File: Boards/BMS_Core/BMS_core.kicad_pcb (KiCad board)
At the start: 2 copper layers, 61 x 80 mm, 79 parts, among them IC1 ATMEGA16M1, J1 CONN_02X03, J2 B5B-PH-K-S, J3 MM_F_VT_20, J4 MicroFit_V_2, J5 isoSPI-Cutout, K1 G5Q-1A4-DC12, Q1 SSM3K333R, T1 T_LAN_SM91501ALE, U1 MCP2561-E_SN, U2 SN74LVC1G17, U3 LTC6820HMS, U4 MCP6001, U5 MCP6001, U6 MCP6001, U7 SN74LVC1G32, U8 TPS560430YF, Y1 Crystal_SMD

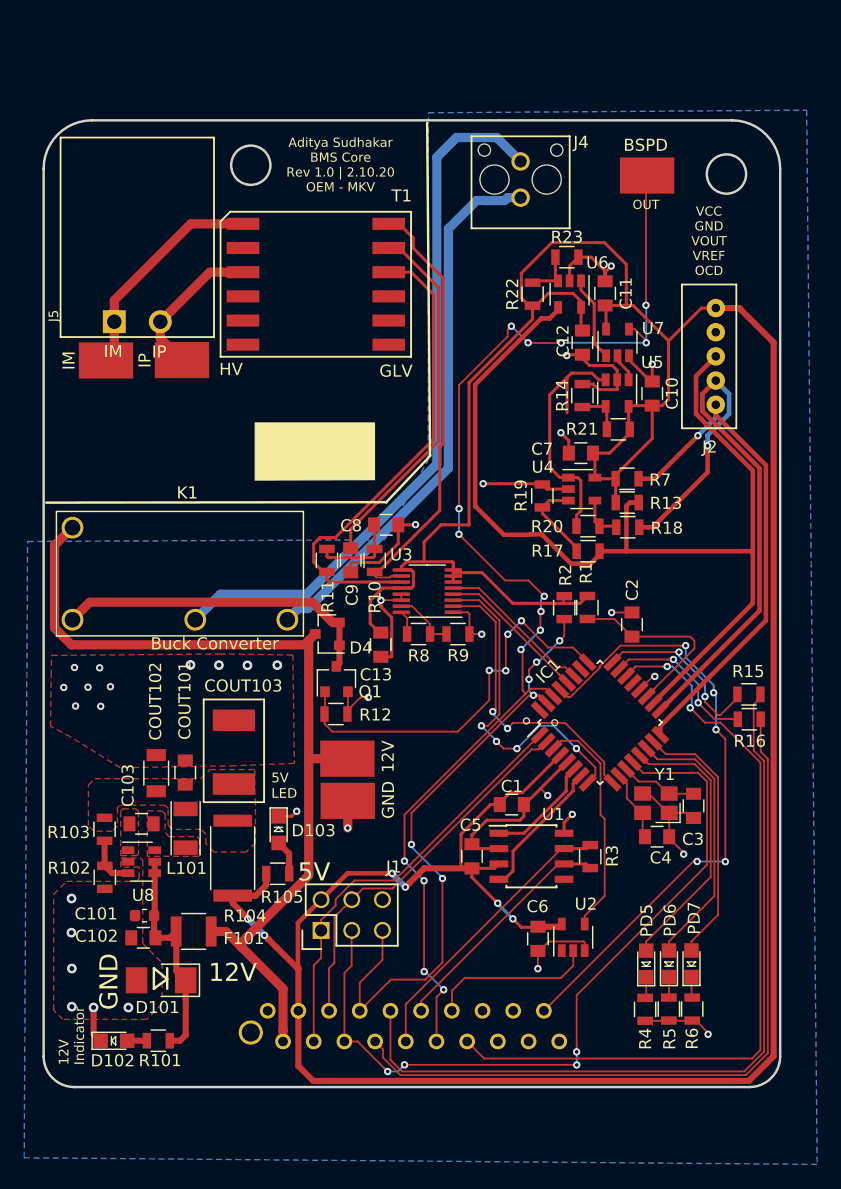
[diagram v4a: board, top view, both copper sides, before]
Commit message: New BMS core DXF, proper GLV HV spacing
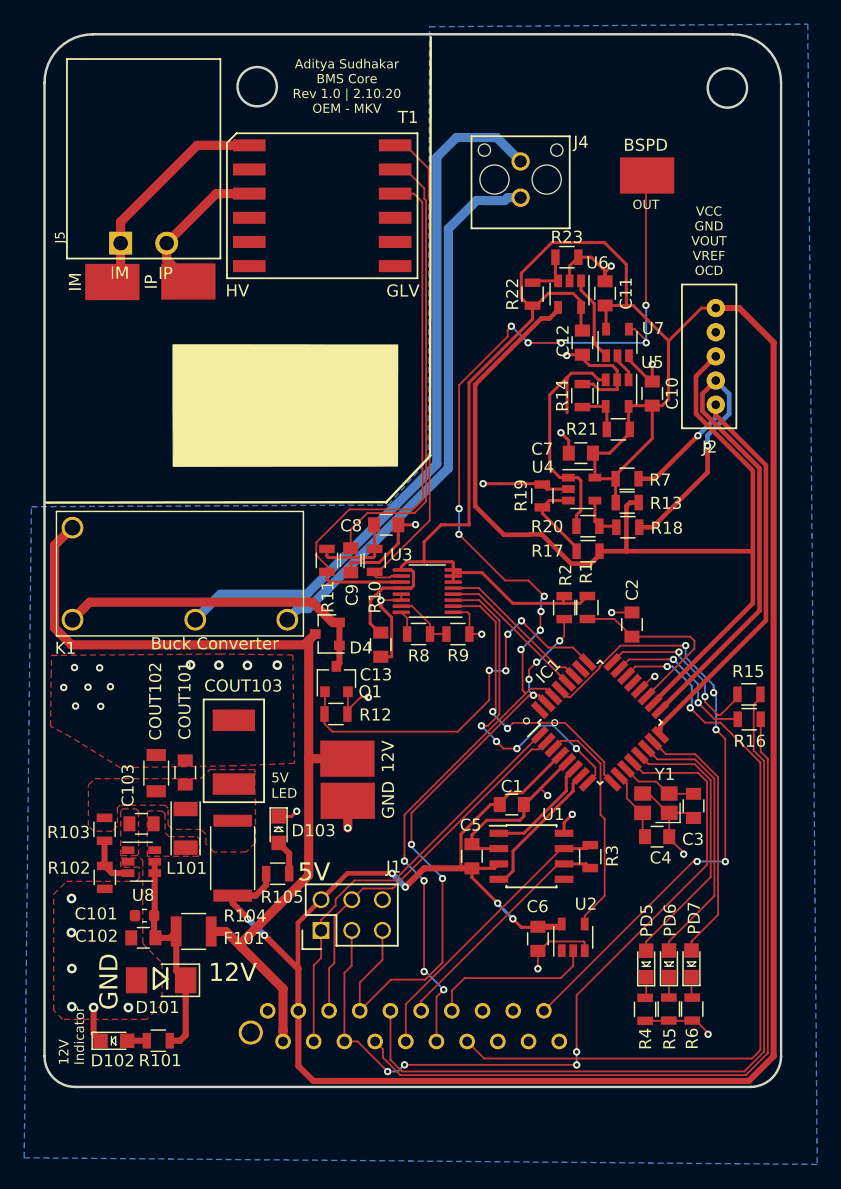
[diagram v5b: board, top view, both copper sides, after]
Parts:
- moved IM 6.52 mm to (36.0, 110.4)
- moved IP 6.52 mm to (42.3, 110.4)
- moved J5 6.52 mm to (38.6, 107.2)
- moved T1 6.52 mm to (53.3, 104.1)
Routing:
- net Net-(C9-Pad1): track 30.0 -> 37.8 mm
- net Net-(R11-Pad2): track 40.4 -> 47.1 mm
- net Net-(R10-Pad1): track 36.3 -> 41.7 mm
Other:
- board size 61 x 80 mm -> 61 x 87.1 mm

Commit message: Final, and slight, changes to layout
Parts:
- added CANH: TP, footprints:tp_1.6mm, F.Cu at (65.1, 163.4)
- added CANL: TP, footprints:tp_1.6mm, F.Cu at (67.4, 165.5)
- moved GND 0.65 mm to (55.5, 154.0)
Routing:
- net /CANH: track 23.8 -> 25.2 mm
- net /CANL: track 19.6 -> 20.5 mm
